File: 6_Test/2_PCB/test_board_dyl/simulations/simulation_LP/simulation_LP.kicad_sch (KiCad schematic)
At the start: 3 parts

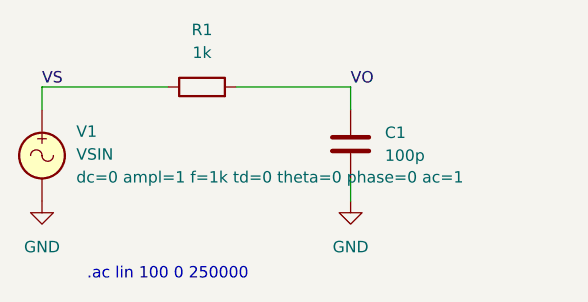
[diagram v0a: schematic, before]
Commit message: Fixed simulation models
Consolidated simulation libraries into sim_models folder in my simulations folder and adjusted file names to be relative paths
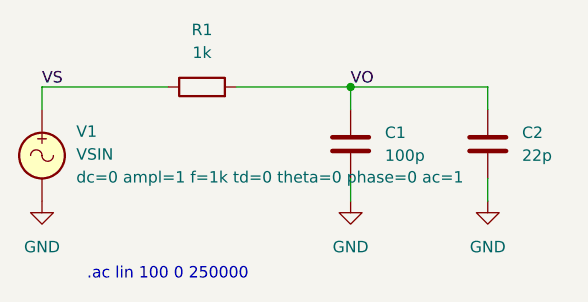
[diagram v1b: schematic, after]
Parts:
- added C2: 22p, symbol Device:C
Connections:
- net GND: now also C2.2
- net VO: now also C2.1
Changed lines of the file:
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@@
 	(generator_version "8.0")
 	(paper "A4")
+	(junction
+		(at 107.95 86.36)
+		(diameter 0)
+		(color 0 0 0 0)
+	)
 	(wire
 		(pts
@@
 	(wire
 		(pts
+			(xy 123.19 96.52) (xy 123.19 99.06)
+		)
+		(stroke
+			(width 0)
+			(type default)
+		)
+	)
+	(wire
+		(pts
+			(xy 123.19 88.9) (xy 123.19 86.36)
+		)
+		(stroke
+			(width 0)
+			(type default)
+		)
+	)
+	(wire
+		(pts
 			(xy 107.95 96.52) (xy 107.95 99.06)
 		)
@@
 		(pts
 			(xy 95.25 86.36) (xy 107.95 86.36)
+		)
+		(stroke
+			(width 0)
+			(type default)
+		)
+	)
+	(wire
+		(pts
+			(xy 123.19 86.36) (xy 107.95 86.36)
 		)
 		(stroke
@@
 			)
 			(justify left bottom)
+		)
+	)
+	(symbol
+		(lib_id "power:GND")
+		(at 123.19 99.06 0)
+		(unit 1)
+		(exclude_from_sim no)
+		(in_bom yes)
+		(on_board yes)
+		(dnp no)
+		(fields_autoplaced yes)
+		(property "Reference" "#PWR03"
+			(at 123.19 105.41 0)
+			(effects
+				(font
+					(size 1.27 1.27)
+				)
+				(hide yes)
+			)
+		)
+		(property "Value" "GND"
+			(at 123.19 104.14 0)
+			(effects
+				(font
+					(size 1.27 1.27)
+				)
+			)
+		)
+		(property "Footprint" ""
+			(at 123.19 99.06 0)
+			(effects
+				(font
+					(size 1.27 1.27)
+				)
+				(hide yes)
+			)
+		)
+		(property "Datasheet" ""
+			(at 123.19 99.06 0)
+			(effects
+				(font
+					(size 1.27 1.27)
+				)
+				(hide yes)
+			)
+		)
+		(property "Description" "Power symbol creates a global label with name \"GND\" , ground"
+			(at 123.19 99.06 0)
+			(effects
+				(font
+					(size 1.27 1.27)
+				)
+				(hide yes)
+			)
+		)
+		(pin "1"
+		)
+		(instances
+			(project "simulation_LP"
+				(path "/589b09a6-41a3-433f-8cae-dd5c7d8e3ac7"
+					(reference "#PWR03")
+					(unit 1)
+				)
+			)
 		)
 	)
@@
 					(unit 1)
 				)
+			)
+		)
+	)
+	(symbol
+		(lib_id "Device:C")
+		(at 123.19 92.71 0)
+		(unit 1)
+		(exclude_from_sim no)
+		(in_bom yes)
+		(on_board yes)
+		(dnp no)
+		(fields_autoplaced yes)
+		(property "Reference" "C2"
+			(at 127 91.4399 0)
+			(effects
+				(font
+					(size 1.27 1.27)
+				)
+				(justify left)
+			)
+		)
+		(property "Value" "22p"
+			(at 127 93.9799 0)
+			(effects
+				(font
+					(size 1.27 1.27)
+				)
+				(justify left)
+			)
+		)
+		(property "Footprint" ""
+			(at 124.1552 96.52 0)
+			(effects
+				(font
+					(size 1.27 1.27)
+				)
+				(hide yes)
+			)
+		)
+		(property "Datasheet" "~"
+			(at 123.19 92.71 0)
+			(effects
+				(font
+					(size 1.27 1.27)
+				)
+				(hide yes)
+			)
+		)
+		(property "Description" "Unpolarized capacitor"
+			(at 123.19 92.71 0)
+			(effects
+				(font
+					(size 1.27 1.27)
+				)
+				(hide yes)
+			)
+		)
+		(pin "2"
+		)
+		(pin "1"
+		)
+		(instances
+			(project "simulation_LP"
+				(path "/589b09a6-41a3-433f-8cae-dd5c7d8e3ac7"
+					(reference "C2")
+					(unit 1)
+				)
